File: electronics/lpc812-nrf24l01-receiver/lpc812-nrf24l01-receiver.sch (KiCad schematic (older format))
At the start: 16 parts, among them K1 BAT, K2 CH3, K3 TH, K4 ST, P1 NRF24L01+, SW1 ISP/BIND, U1 MCP1703T-3302E/CB, U2 LPC812M101JDH16_TSSOP16, X1 12 MHz

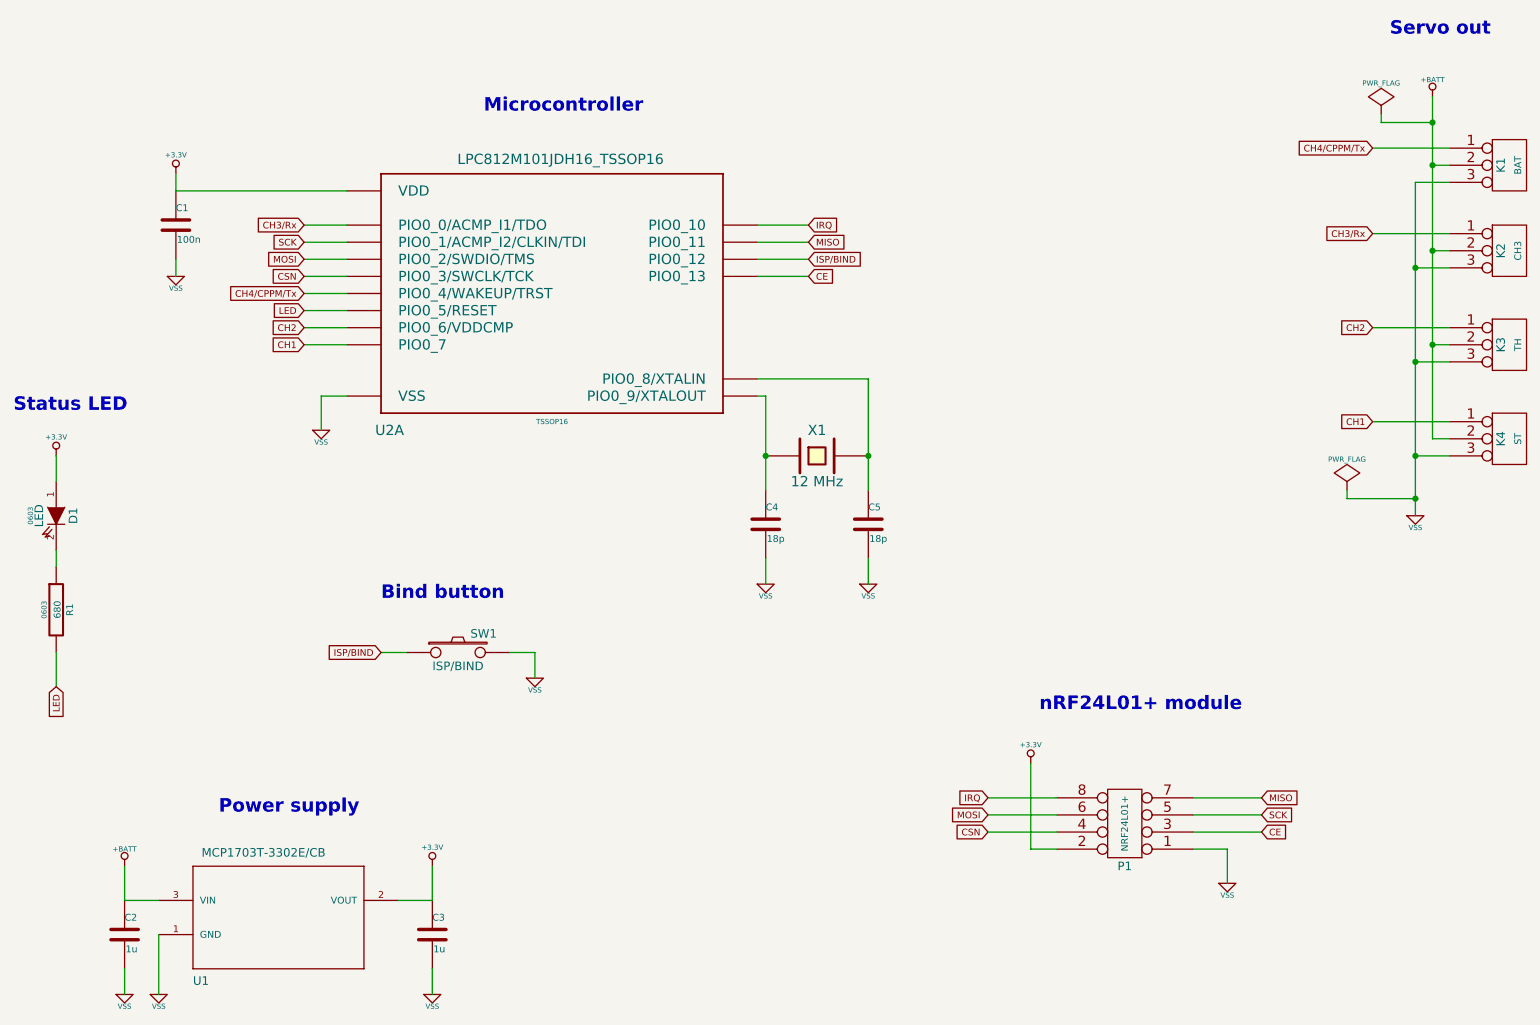
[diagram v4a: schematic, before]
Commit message: Re-layout the board, add protection resistors
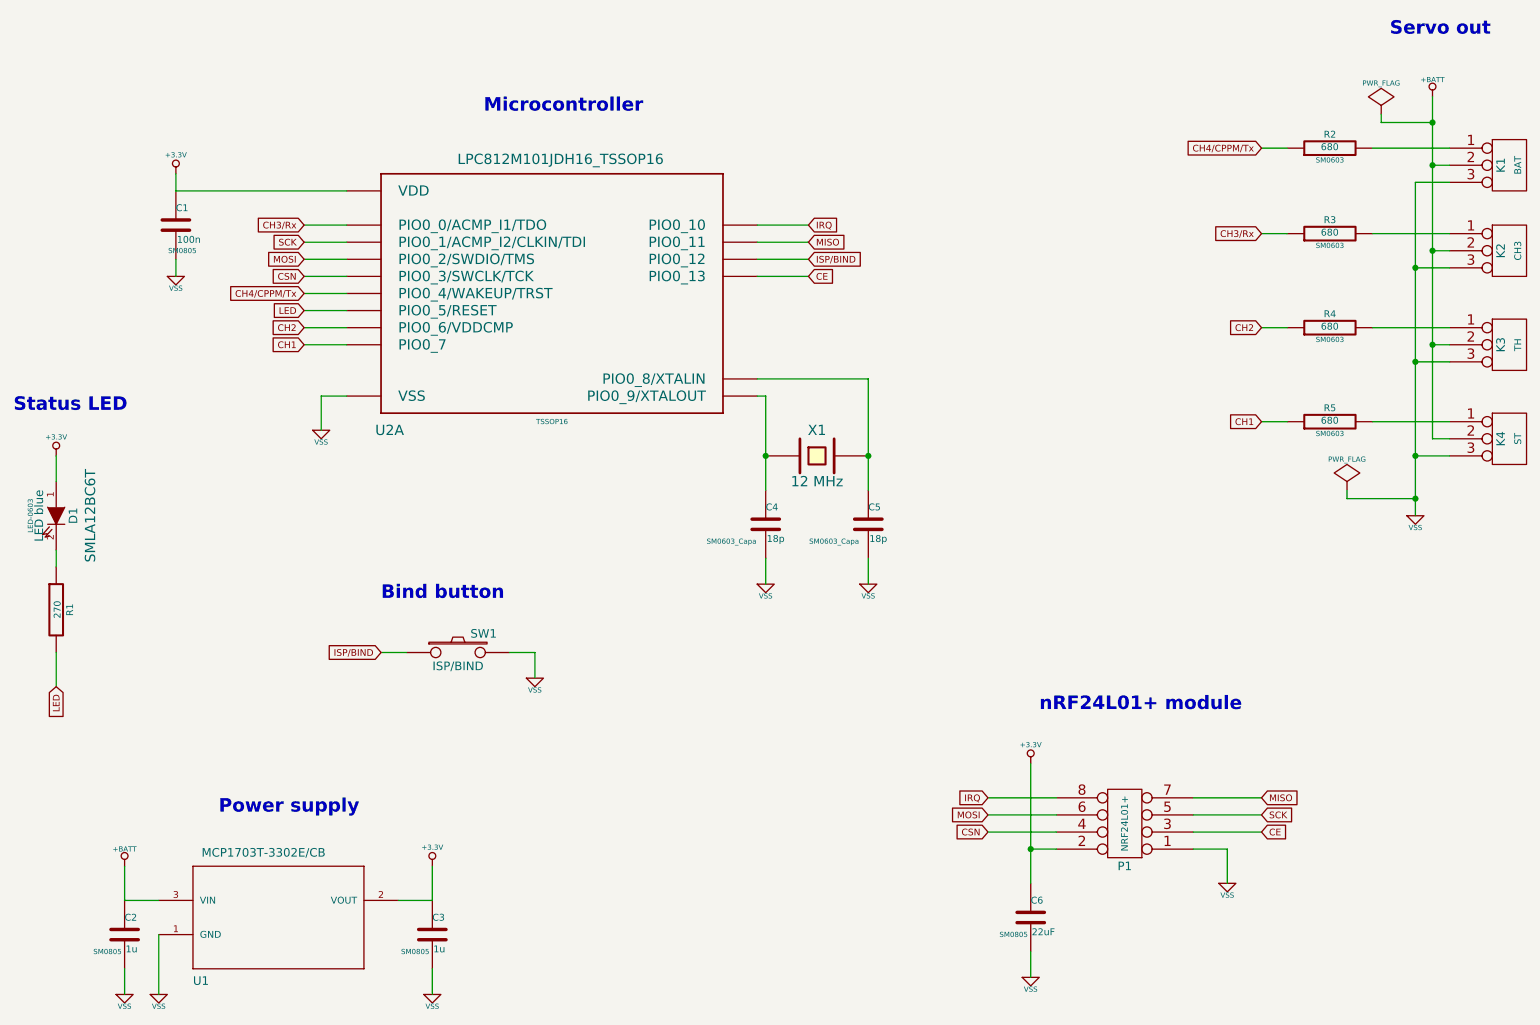
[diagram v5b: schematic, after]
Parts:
- added C6: 22uF, SM0805, symbol C
- added R2, R3, R4, R5: 680, SM0603, symbol R
- C1, C2, C3: footprint ~ -> SM0805
- C4, C5: footprint ~ -> SM0603_Capa
- D1: value LED -> LED blue; footprint 0603 -> LED-0603
- K1, K2, K3, K4: footprint (none) -> PIN_ARRAY_3X1
- P1: footprint (none) -> pin_array_4x2
- R1: value 680 -> 270; footprint 0603 -> SM0603
- SW1: footprint ~ -> SW_PUSH_SMALL
- X1: footprint ~ -> crystal-SM49
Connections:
- net +3.3V: now also C6.1
- net CH1: now also R5.1; no longer K4.1 (P1)
- net CH2: now also R4.1; no longer K3.1 (P1)
- net CH3/Rx: now also R3.1; no longer K2.1 (P1)
- net CH4/CPPM/Tx: now also R2.1; no longer K1.1 (P1)
- net VSS: now also C6.2
- new net: K1.1 (P1), R2.2
- new net: K2.1 (P1), R3.2
- new net: K3.1 (P1), R4.2
- new net: K4.1 (P1), R5.2
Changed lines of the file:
@@
 Sheet 1 1
 Title ""
-Date "22 nov 2014"
+Date "23 nov 2014"
 Rev ""
 Comp ""
@@
 F 0 "P1" H 7950 5850 50  0000 C CNN
 F 1 "NRF24L01+" V 7950 5600 40  0000 C CNN
-F 2 "" H 7950 5600 60  0000 C CNN
+F 2 "pin_array_4x2" H 7950 5600 60  0001 C CNN
 F 3 "" H 7950 5600 60  0000 C CNN
 	1    7950 5600
@@
 F 0 "C3" H 3900 6350 40  0000 L CNN
 F 1 "1u" H 3906 6165 40  0000 L CNN
-F 2 "~" H 3938 6100 30  0000 C CNN
+F 2 "SM0805" H 3800 6150 30  0000 C CNN
 F 3 "~" H 3900 6250 60  0000 C CNN
 	1    3900 6250
@@
 F 0 "C1" H 2400 2200 40  0000 L CNN
 F 1 "100n" H 2406 2015 40  0000 L CNN
-F 2 "~" H 2438 1950 30  0000 C CNN
+F 2 "SM0805" H 2438 1950 30  0000 C CNN
 F 3 "~" H 2400 2100 60  0000 C CNN
 	1    2400 2100
@@
 F 0 "C2" H 2100 6350 40  0000 L CNN
 F 1 "1u" H 2106 6165 40  0000 L CNN
-F 2 "~" H 2138 6100 30  0000 C CNN
+F 2 "SM0805" H 2000 6150 30  0000 C CNN
 F 3 "~" H 2100 6250 60  0000 C CNN
 	1    2100 6250
@@
 F 0 "K1" V 10150 1750 50  0000 C CNN
 F 1 "BAT" V 10250 1750 40  0000 C CNN
-F 2 "" H 10200 1750 60  0000 C CNN
+F 2 "PIN_ARRAY_3X1" H 10200 1750 60  0001 C CNN
 F 3 "" H 10200 1750 60  0000 C CNN
 	1    10200 1750
@@
 F 0 "K2" V 10150 2250 50  0000 C CNN
 F 1 "CH3" V 10250 2250 40  0000 C CNN
-F 2 "" H 10200 2250 60  0000 C CNN
+F 2 "PIN_ARRAY_3X1" H 10200 2250 60  0001 C CNN
 F 3 "" H 10200 2250 60  0000 C CNN
 	1    10200 2250
@@
 F 0 "K3" V 10150 2800 50  0000 C CNN
 F 1 "TH" V 10250 2800 40  0000 C CNN
-F 2 "" H 10200 2800 60  0000 C CNN
+F 2 "PIN_ARRAY_3X1" H 10200 2800 60  0001 C CNN
 F 3 "" H 10200 2800 60  0000 C CNN
 	1    10200 2800
@@
 F 0 "K4" V 10150 3350 50  0000 C CNN
 F 1 "ST" V 10250 3350 40  0000 C CNN
-F 2 "" H 10200 3350 60  0000 C CNN
+F 2 "PIN_ARRAY_3X1" H 10200 3350 60  0001 C CNN
 F 3 "" H 10200 3350 60  0000 C CNN
 	1    10200 3350
@@
 Text GLabel 6100 2200 2    39   Input ~ 0
 MISO
-Text GLabel 9400 2150 0    39   Input ~ 0
+Text GLabel 8750 2150 0    39   Input ~ 0
 CH3/Rx
-Text GLabel 9400 2700 0    39   Input ~ 0
+Text GLabel 8750 2700 0    39   Input ~ 0
 CH2
-Text GLabel 9400 3250 0    39   Input ~ 0
+Text GLabel 8750 3250 0    39   Input ~ 0
 CH1
 Text GLabel 6100 2300 2    39   Input ~ 0
@@
 F 0 "X1" H 6150 3600 60  0000 C CNN
 F 1 "12 MHz" H 6150 3300 60  0000 C CNN
-F 2 "~" H 6150 3450 60  0000 C CNN
+F 2 "crystal-SM49" H 6150 3450 60  0001 C CNN
 F 3 "~" H 6150 3450 60  0000 C CNN
 	1    6150 3450
@@
 F 0 "C4" H 5850 3950 40  0000 L CNN
 F 1 "18p" H 5856 3765 40  0000 L CNN
-F 2 "~" H 5888 3700 30  0000 C CNN
+F 2 "SM0603_Capa" H 5650 3750 30  0000 C CNN
 F 3 "~" H 5850 3850 60  0000 C CNN
 	1    5850 3850
@@
 F 0 "C5" H 6450 3950 40  0000 L CNN
 F 1 "18p" H 6456 3765 40  0000 L CNN
-F 2 "~" H 6488 3700 30  0000 C CNN
+F 2 "SM0603_Capa" H 6250 3750 30  0000 C CNN
 F 3 "~" H 6450 3850 60  0000 C CNN
 	1    6450 3850
@@
 Text GLabel 3150 2800 0    39   Input ~ 0
 CH1
-Text GLabel 9400 1650 0    39   Input ~ 0
+Text GLabel 8750 1650 0    39   Input ~ 0
 CH4/CPPM/Tx
 $Comp
@@
 F 0 "SW1" H 4200 4710 50  0000 C CNN
 F 1 "ISP/BIND" H 4050 4520 50  0000 C CNN
-F 2 "~" H 4050 4600 60  0000 C CNN
+F 2 "SW_PUSH_SMALL" H 4050 4600 60  0001 C CNN
 F 3 "~" H 4050 4600 60  0000 C CNN
 	1    4050 4600
@@
 P 1700 3800
 F 0 "D1" H 1700 3900 50  0000 C CNN
-F 1 "LED" H 1700 3700 50  0000 C CNN
-F 2 "0603" H 1700 3650 30  0000 C CNN
-F 3 "~" H 1700 3800 60  0000 C CNN
+F 1 "LED blue" H 1700 3700 50  0000 C CNN
+F 2 "LED-0603" H 1700 3650 30  0000 C CNN
+F 3 "SMLA12BC6T" H 1700 4000 60  0000 C CNN
 	1    1700 3800
 	0    1    1    0
@@
 P 1700 4350
 F 0 "R1" V 1780 4350 40  0000 C CNN
-F 1 "680" V 1707 4351 40  0000 C CNN
-F 2 "0603" V 1630 4350 30  0000 C CNN
+F 1 "270" V 1707 4351 40  0000 C CNN
+F 2 "SM0603" V 1630 4350 30  0001 C CNN
 F 3 "~" H 1700 4350 30  0000 C CNN
 	1    1700 4350
@@
 	8550 5750 8550 5950
 Wire Wire Line
-	7400 5250 7400 5750
+	7400 5250 7400 5950
 Wire Wire Line
 	7400 5750 7550 5750
@@
 	9450 1500 9750 1500
 Connection ~ 9750 1500
+$Comp
+L C C6
+U 1 1 5471B4BB
+P 7400 6150
+F 0 "C6" H 7400 6250 40  0000 L CNN
+F 1 "22uF" H 7406 6065 40  0000 L CNN
+F 2 "SM0805" H 7300 6050 30  0000 C CNN
+F 3 "~" H 7400 6150 60  0000 C CNN
+	1    7400 6150
+	1    0    0    -1
+$EndComp
+Connection ~ 7400 5750
+$Comp
+L VSS #PWR019
+U 1 1 5471B56E
+P 7400 6500
+F 0 "#PWR019" H 7400 6500 30  0001 C CNN
+F 1 "VSS" H 7400 6430 30  0000 C CNN
+F 2 "" H 7400 6500 60  0000 C CNN
+F 3 "" H 7400 6500 60  0000 C CNN
+	1    7400 6500
+	1    0    0    -1
+$EndComp
+Wire Wire Line
+	7400 6350 7400 6500
+$Comp
+L R R2
+U 1 1 5471D01E
+P 9150 1650
+F 0 "R2" V 9230 1650 40  0000 C CNN
+F 1 "680" V 9157 1651 40  0000 C CNN
+F 2 "SM0603" V 9080 1650 30  0000 C CNN
+F 3 "~" H 9150 1650 30  0000 C CNN
+	1    9150 1650
+	0    -1   -1   0
+$EndComp
+$Comp
+L R R3
+U 1 1 5471D02B
+P 9150 2150
+F 0 "R3" V 9230 2150 40  0000 C CNN
+F 1 "680" V 9157 2151 40  0000 C CNN
+F 2 "SM0603" V 9080 2150 30  0000 C CNN
+F 3 "~" H 9150 2150 30  0000 C CNN
+	1    9150 2150
+	0    -1   -1   0
+$EndComp
+$Comp
+L R R4
+U 1 1 5471D031
+P 9150 2700
+F 0 "R4" V 9230 2700 40  0000 C CNN
+F 1 "680" V 9157 2701 40  0000 C CNN
+F 2 "SM0603" V 9080 2700 30  0000 C CNN
+F 3 "~" H 9150 2700 30  0000 C CNN
+	1    9150 2700
+	0    -1   -1   0
+$EndComp
+$Comp
+L R R5
+U 1 1 5471D037
+P 9150 3250
+F 0 "R5" V 9230 3250 40  0000 C CNN
+F 1 "680" V 9157 3251 40  0000 C CNN
+F 2 "SM0603" V 9080 3250 30  0000 C CNN
+F 3 "~" H 9150 3250 30  0000 C CNN
+	1    9150 3250
+	0    -1   -1   0
+$EndComp
+Wire Wire Line
+	8750 3250 8900 3250
+Wire Wire Line
+	8750 2700 8900 2700
+Wire Wire Line
+	8750 2150 8900 2150
+Wire Wire Line
+	8750 1650 8900 1650
 $EndSCHEMATC

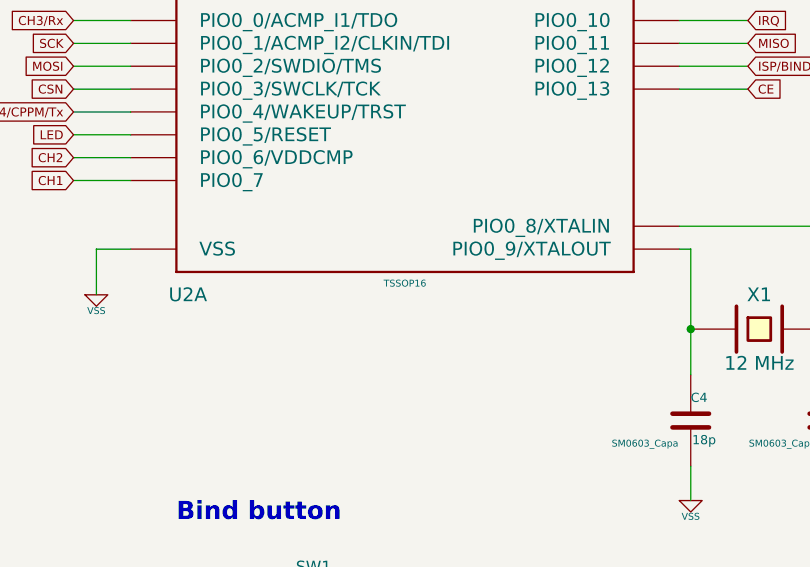
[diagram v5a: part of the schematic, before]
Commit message: Tweak the board and use NXP footprints
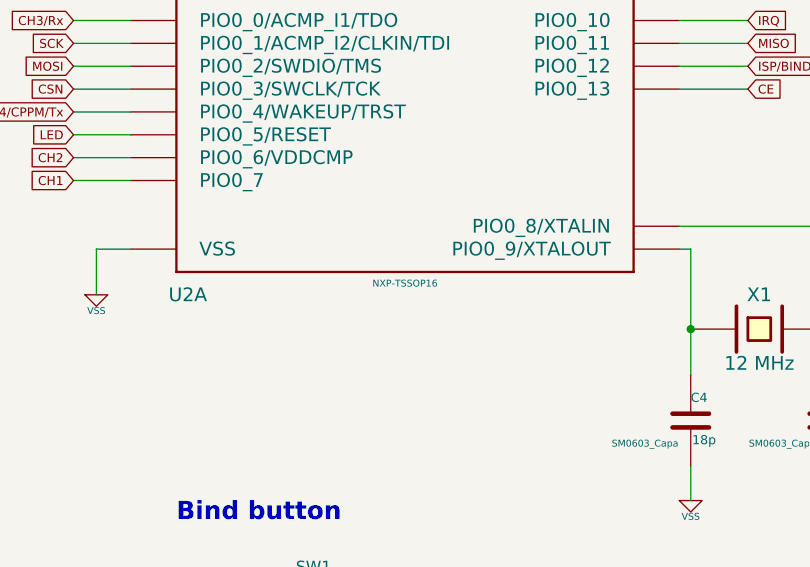
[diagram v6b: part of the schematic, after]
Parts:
- U2: footprint TSSOP16 -> NXP-TSSOP16
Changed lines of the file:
@@
 F 0 "U2" H 3650 1600 60  0000 C CNN
 F 1 "LPC812M101JDH16_TSSOP16" H 4650 3150 60  0000 C BNN
-F 2 "TSSOP16" H 4600 1650 30  0000 C CNN
+F 2 "NXP-TSSOP16" H 4600 1650 30  0000 C CNN
 F 3 "" H 4600 2450 60  0000 C CNN
 	1    4600 2450
